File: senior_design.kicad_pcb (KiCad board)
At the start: 2 copper layers, 128.6 x 80.8 mm, 131 parts, among them J10 Conn_01x01_Pin, J11 Conn_01x01_Pin, J12 Conn_01x01_Pin, J13 Conn_ARM_JTAG_SWD_10, J2 Conn_01x03_Pin, J3 Conn_01x09_Socket, J4 USB_B_Micro, J5 Out_to_display, J6 AudioJack3, J7 SD_Card_Receptacle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

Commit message: small changes
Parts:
- added C36: 6.8nF, Capacitor_SMD:C_0805_2012Metric_Pad1.18x1.45mm_HandSolder, B.Cu at (168.5, 92.6)
- added C37: 10 uF, Capacitor_SMD:C_0805_2012Metric_Pad1.18x1.45mm_HandSolder, B.Cu at (164.6, 93.5)
- added R51: 1k, Resistor_SMD:R_0805_2012Metric_Pad1.20x1.40mm_HandSolder, B.Cu at (172.2, 93.6)
- moved J10 1.43 mm to (152.5, 97.0)
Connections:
- D8 pad 2: /Audio/AUDIO_IN -> Net-(D8-A2)
- J6 pad R: /Audio/AUDIO_IN -> Net-(D8-A2)
- J6 pad T: /Audio/AUDIO_IN -> Net-(D8-A2)
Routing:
- net /Audio/AUDIO_IN: track 68.3 -> 15.7 mm, vias 2 -> 1
- net Net-(D8-A2): track 0.00 -> 44.4 mm, vias 0 -> 1
- net Net-(C36-Pad1): track 0.00 -> 5.71 mm
- net Net-(U13-+): track 15.7 -> 17.1 mm
- net /Hall Effect/ADC_IN2: track 56.0 -> 57.3 mm
- net CORE_VDD: track 47.3 -> 46.2 mm, vias 7 -> 6
- net /Hall Effect/ADC_IN1: track 59.5 -> 60.6 mm
- net Net-(U12-+): track 8.04 -> 9.08 mm
- net Net-(R11-Pad1): track 8.77 -> 9.67 mm
- net Net-(U12--): track 8.16 -> 8.84 mm
- net Net-(U4-+): track 15.8 -> 16.4 mm

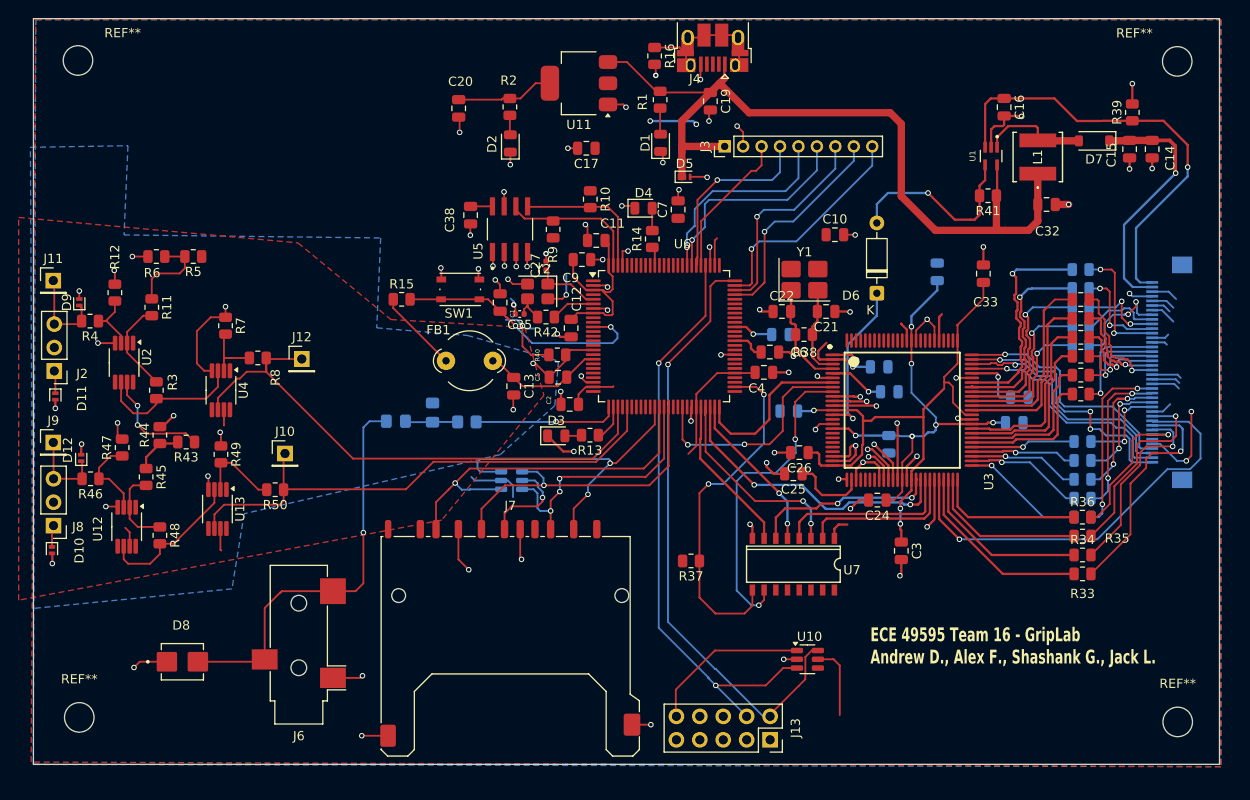
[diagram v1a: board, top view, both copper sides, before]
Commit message: Updated Constraints for NextPCB
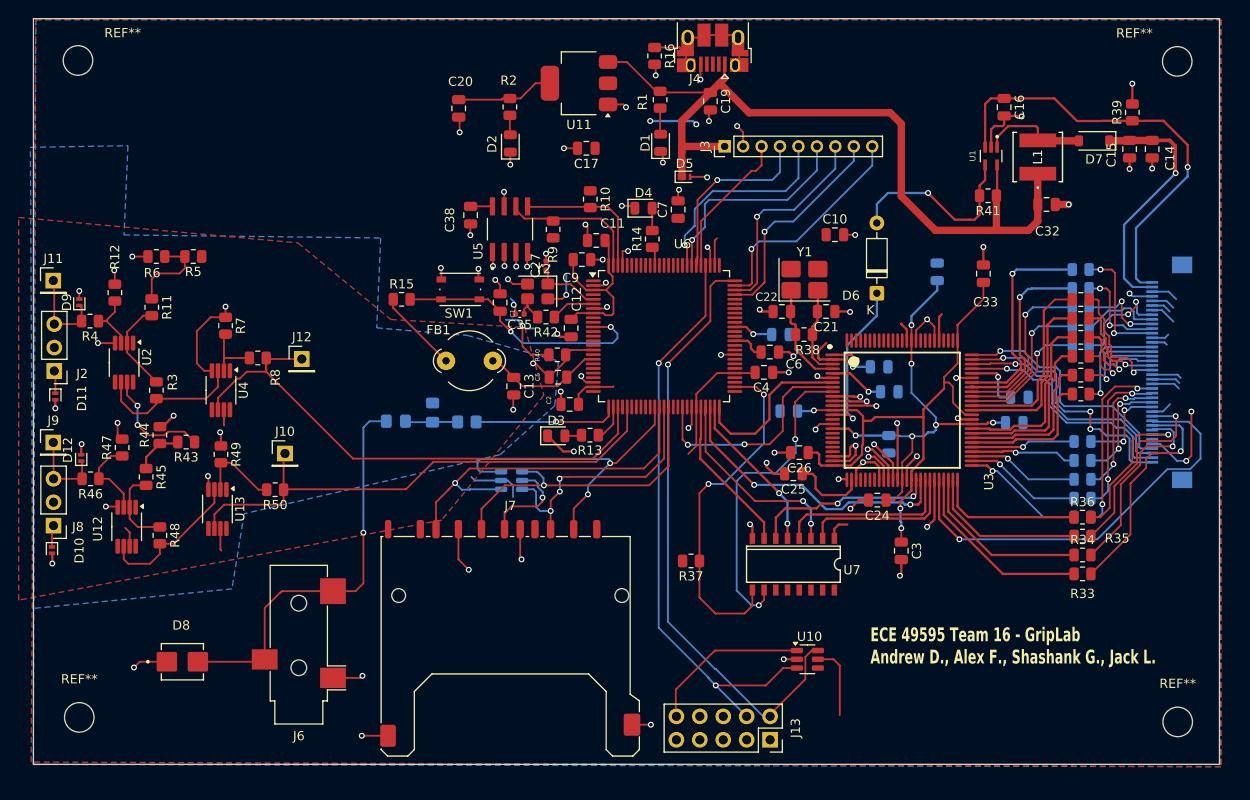
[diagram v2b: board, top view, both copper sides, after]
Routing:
- net +3.3V: track 188.5 -> 187.0 mm
- net Net-(U3-PDAT12): track 17.9 -> 16.5 mm
- net Net-(U3-PDAT11): track 15.9 -> 14.6 mm
- net GND: track 237.4 -> 238.6 mm
- net Net-(U3-PDAT13): track 19.8 -> 18.7 mm
- net Net-(U3-PDAT14): track 21.7 -> 20.8 mm
- net /Peripherals/B5: track 15.3 -> 14.4 mm
- net /Peripherals/G3: track 9.30 -> 10.1 mm
- net /Peripherals/G4: track 9.56 -> 10.3 mm
- net Net-(U3-PDAT15): track 24.0 -> 23.3 mm
- net /MCU/SWD_RESET: track 28.2 -> 28.8 mm

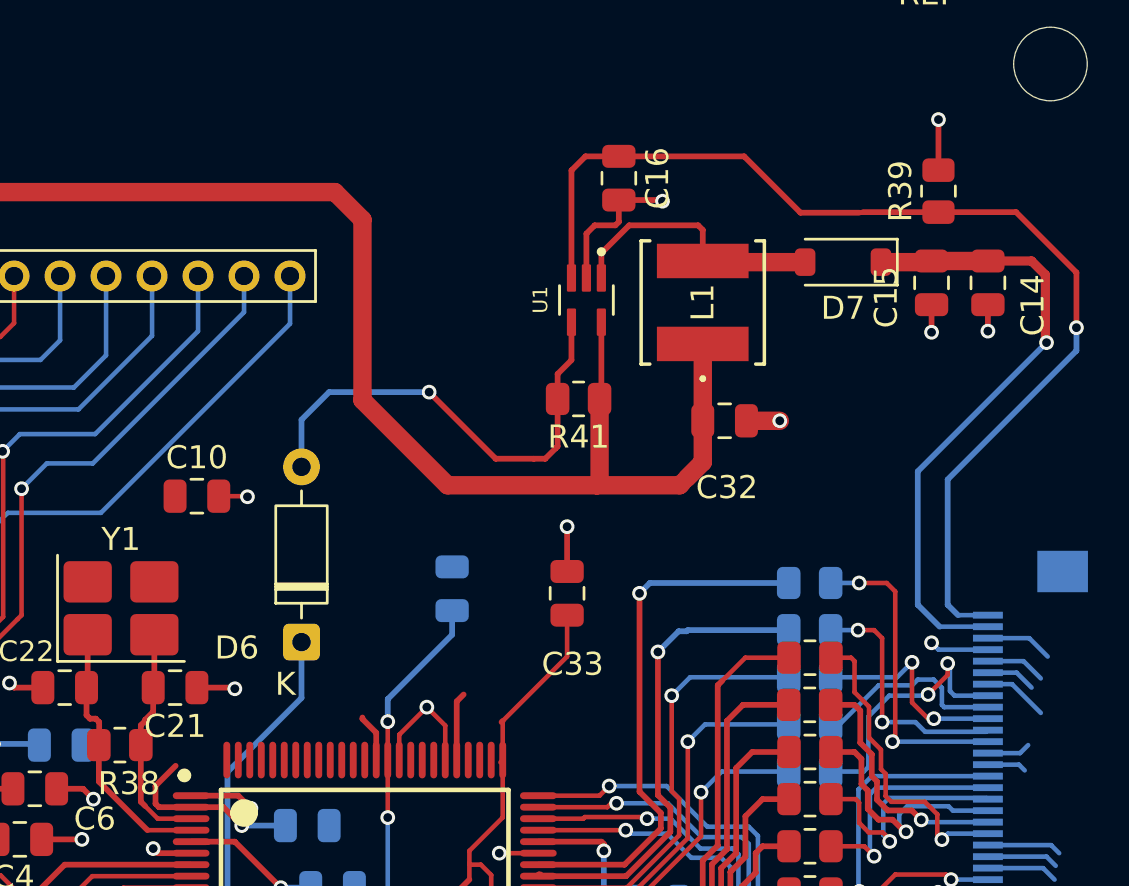
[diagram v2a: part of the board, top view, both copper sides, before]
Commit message: Boost converter plane edit
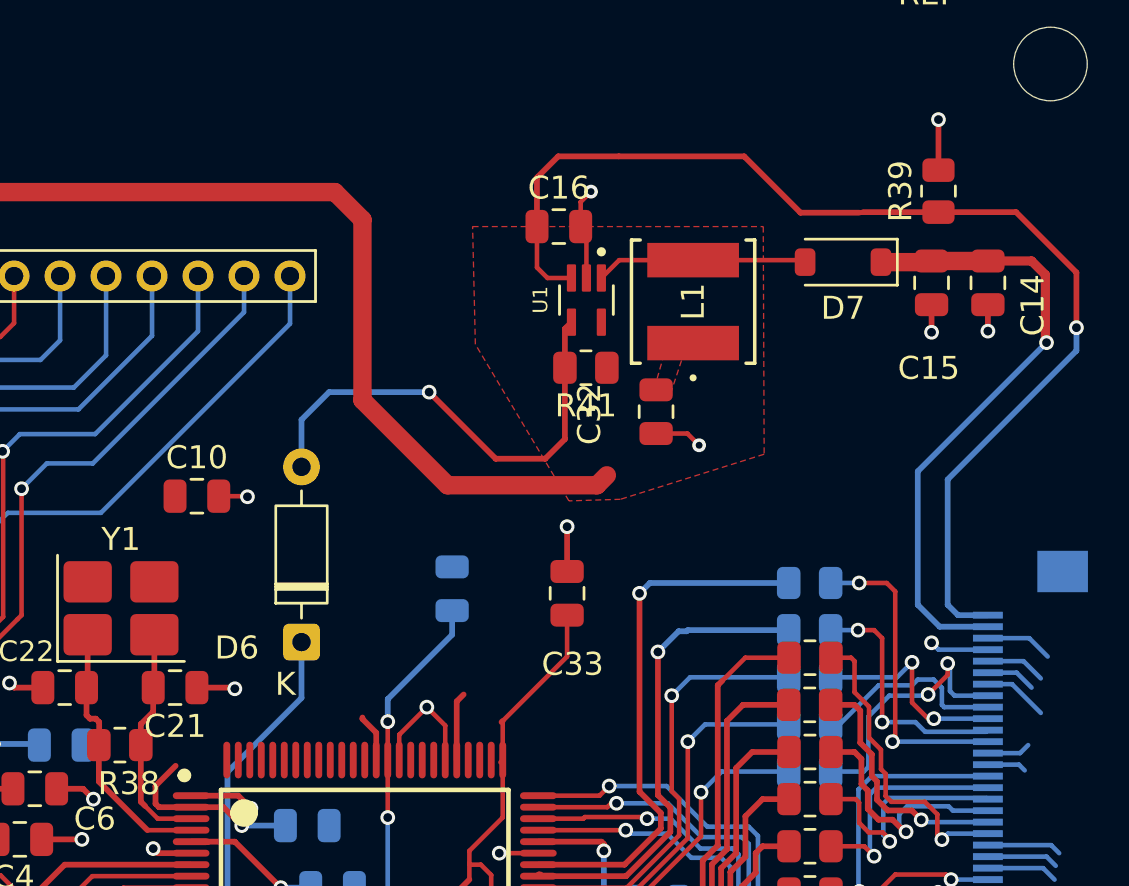
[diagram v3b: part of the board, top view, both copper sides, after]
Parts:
- moved C16 3.35 mm to (227.9, 61.6), turned to 0 degrees
- moved C32 3.01 mm to (232.1, 69.7), turned to -90 degrees
- moved R41 1.39 mm to (229.1, 67.7)
- moved L1 0.42 mm to (233.7, 64.9)
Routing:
- net +5V: track 90.2 -> 73.5 mm
- net Net-(D7-A): track 11.9 -> 9.29 mm
- net /Peripherals/LEDK: track 47.9 -> 50.4 mm
- net GND: track 238.6 -> 236.9 mm
- added copper zone on F.Cu, net +5V

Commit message: plane and jumper fix
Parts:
- removed U9: WE-TVS-824015043, Package_TO_SOT_SMD:SOT-23-6
- moved C36 20.9 mm to (155.9, 109.3), turned to 180 degrees
- moved C37 19.2 mm to (161.1, 112.4), turned to -90 degrees
- moved R51 18.5 mm to (161.1, 108.3), turned to -90 degrees
- moved D8 3.85 mm to (141.5, 123.5)
- moved J6 3.85 mm to (154.1, 121.6)
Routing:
- net /Audio/AUDIO_IN: track 15.7 -> 34.8 mm
- net /MCU/SPI4_CS: track 35.6 -> 17.3 mm
- net Net-(D8-A2): track 44.4 -> 26.4 mm
- net GND: track 236.9 -> 230.6 mm
- net /MCU/SPI4_SCK: track 39.6 -> 34.3 mm, vias 1 -> 0
- net /MCU/SPI4_MISO: track 28.8 -> 23.8 mm, vias 3 -> 2
- net +3.3V: track 187.0 -> 183.4 mm, vias 9 -> 8
- net /MCU/SPI4_MOSI: track 34.3 -> 30.8 mm, vias 1 -> 0
- net GNDA: track 38.4 -> 41.4 mm

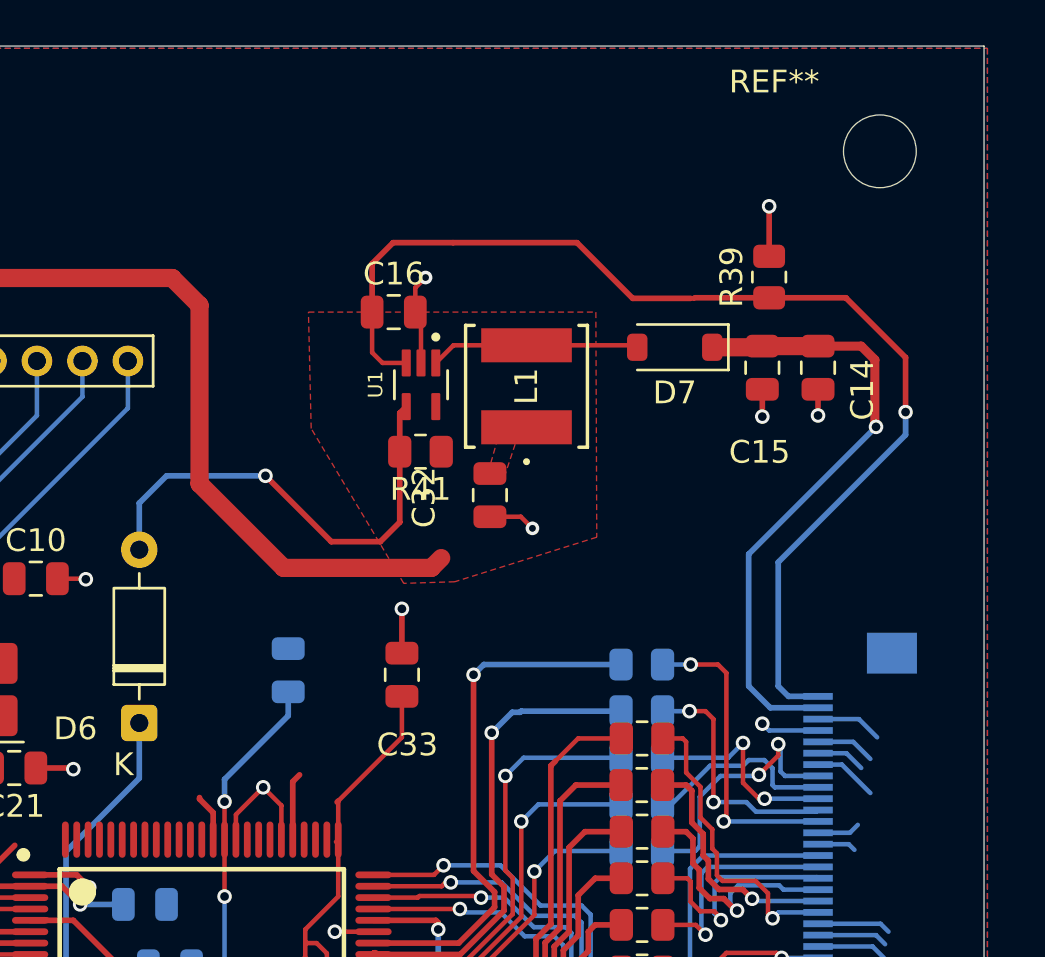
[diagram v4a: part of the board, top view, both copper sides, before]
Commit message: boost converter
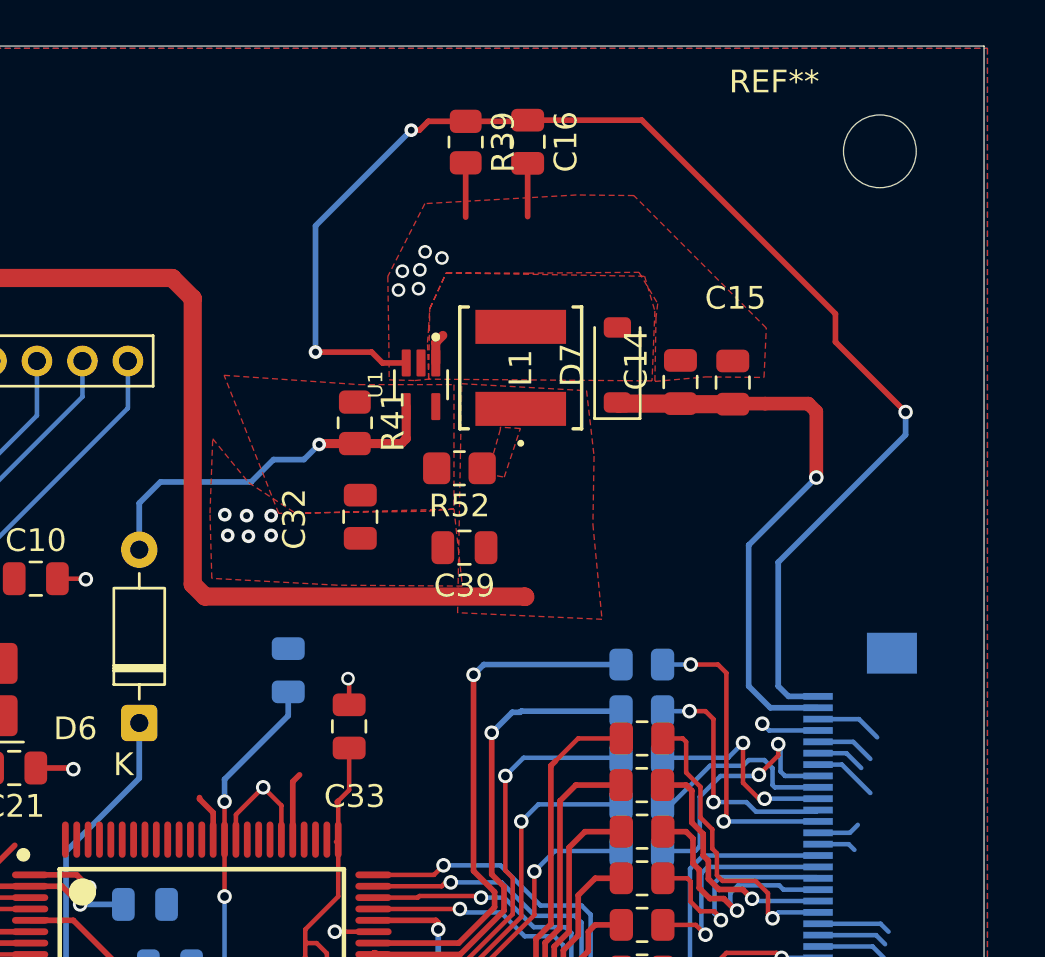
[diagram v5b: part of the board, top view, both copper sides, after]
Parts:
- added C39: 10uF, Capacitor_SMD:C_0805_2012Metric, F.Cu at (231.0, 72.0)
- added R52: 10, Resistor_SMD:R_0805_2012Metric_Pad1.20x1.40mm_HandSolder, F.Cu at (230.8, 68.5)
- C32: value 10uF -> 1uF
- R39: value 10k -> 10
- moved R39 14.6 mm to (231.1, 54.1), turned to -90 degrees
- moved C16 9.53 mm to (233.8, 54.1), turned to -90 degrees
- moved C14 6.08 mm to (240.5, 64.7), turned to 90 degrees
- moved C32 5.78 mm to (226.4, 70.6)
- moved C33 3.25 mm to (225.9, 79.8)
- moved R41 3.15 mm to (226.2, 66.5), turned to -90 degrees
- moved D7 2.64 mm to (237.7, 63.9), turned to 90 degrees
- moved C15 1.45 mm to (242.8, 64.7), turned to 90 degrees
- moved L1 0.85 mm to (233.5, 64.1)
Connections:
- C32 pad 1: +5V -> Net-(U1-VIN)
- R41 pad 1: +5V -> Net-(U1-VIN)
- U1 pad 5: +5V -> Net-(U1-VIN)
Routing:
- net /Peripherals/LEDK: track 50.4 -> 60.0 mm, vias 1 -> 3
- net Net-(D7-A): track 9.29 -> 1.34 mm
- net +5V: track 73.5 -> 80.3 mm
- net GND: track 230.6 -> 223.8 mm, vias 81 -> 88
- net Net-(D6-A): track 20.8 -> 16.4 mm
- net +3.3V: track 183.4 -> 180.1 mm
- net +24V: track 27.7 -> 25.9 mm
- added copper zone on F.Cu, net GND
- added copper zone on F.Cu, net Net-(D7-A)
- added copper zone on F.Cu, net Net-(U1-VIN)

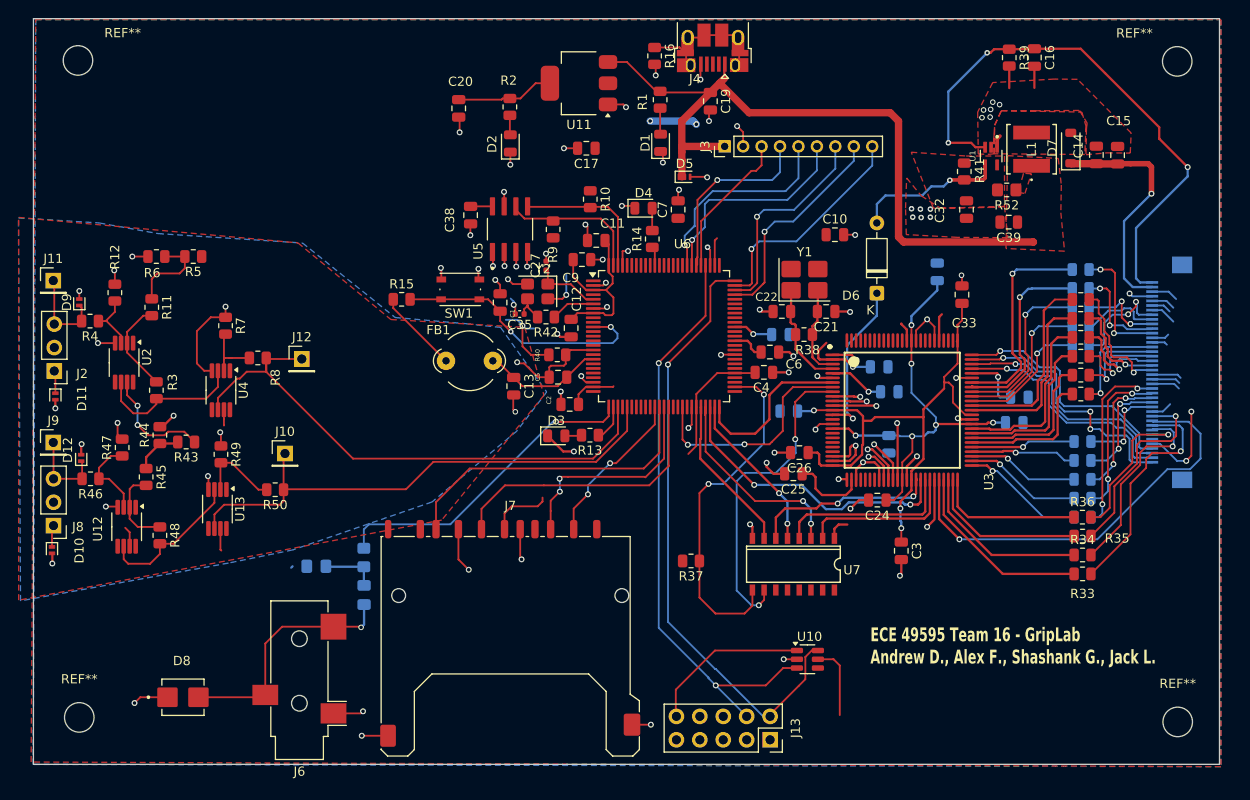
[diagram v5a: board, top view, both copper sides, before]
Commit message: boost converter
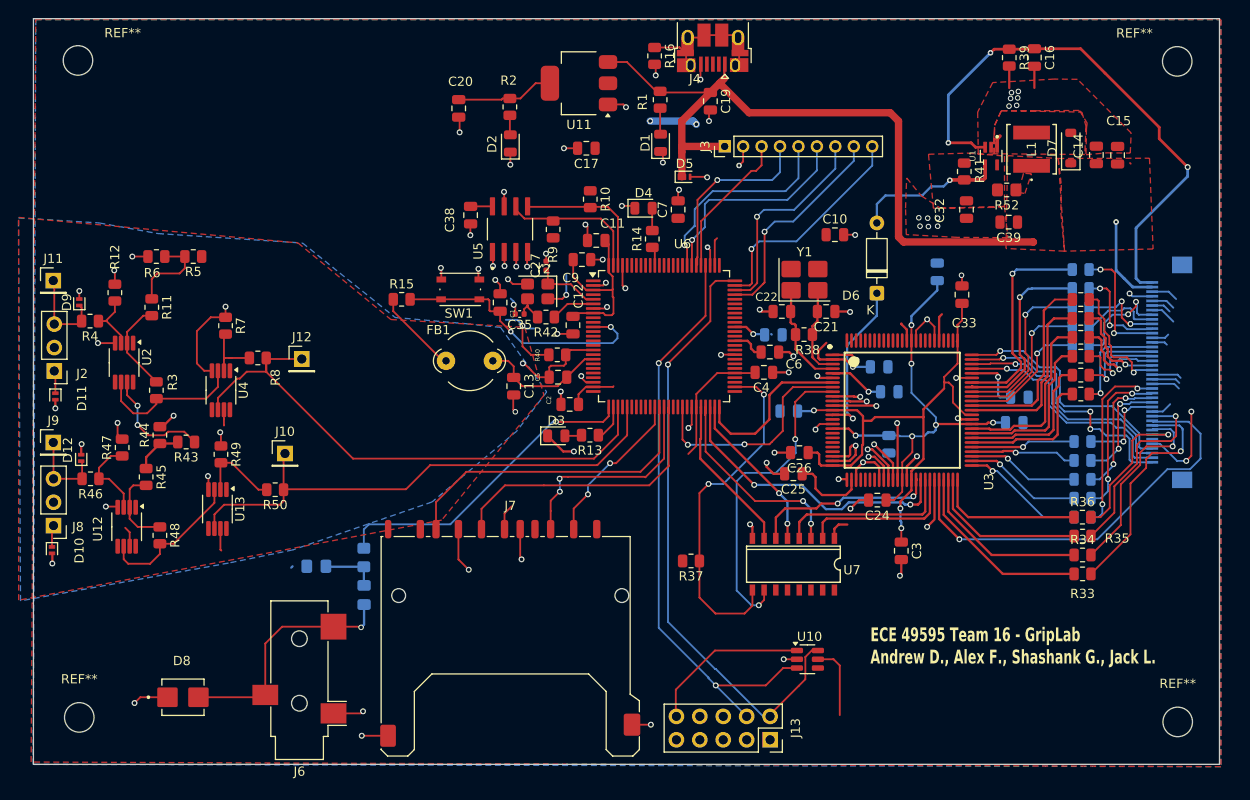
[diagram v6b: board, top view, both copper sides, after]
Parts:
- moved C8 0.77 mm to (205.5, 84.2)
- moved C12 0.38 mm to (183.8, 83.1)
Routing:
- net +24V: track 25.9 -> 10.3 mm
- net +3.3V: track 180.1 -> 175.5 mm
- net VDDA: track 37.8 -> 38.5 mm
- net GNDA: track 41.4 -> 40.7 mm
- net /MCU/SWD_RESET: track 28.8 -> 29.4 mm
- added copper zone on F.Cu, net +24V

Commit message: Feedback Final Update
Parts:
- added D13: D_Schottky, SS14 Schottky:DIONM4336X250N, F.Cu at (202.3, 59.6)
- moved D5 14.5 mm to (207.1, 57.9)
- moved C19 4.36 mm to (194.3, 58.6)
- moved J3 2.66 mm to (198.5, 65.8)
- moved R1 1.50 mm to (191.7, 58.6)
- moved D1 1.50 mm to (191.8, 63.3)
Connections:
- D5 pad 1: +5V -> Net-(D13-A)
- J4 pad 1: +5V -> Net-(D13-A)
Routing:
- net +5V: track 80.3 -> 65.1 mm
- net Net-(D13-A): track 0.00 -> 9.48 mm
- net /MCU/MOSI2: track 22.8 -> 18.7 mm
- net /MCU/CS2: track 15.9 -> 12.9 mm
- net +3.3V: track 175.5 -> 178.4 mm
- net /MCU/SCK2: track 20.1 -> 17.3 mm
- net /MCU/SPI4_RST: track 23.0 -> 20.3 mm
- net /MCU/SPI4_WAIT: track 23.7 -> 20.9 mm
- net /MCU/MISO2: track 23.5 -> 20.7 mm
- net /MCU/SPI4_INT: track 24.6 -> 23.0 mm
- net GND: track 224.1 -> 223.0 mm
